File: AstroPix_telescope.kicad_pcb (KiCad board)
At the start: 4 copper layers, 84.3 x 96.1 mm, 14 parts, among them J1 AstroPix2_pcie, J2 AstroPix2_pcie, J3 AstroPix2_pcie, J4 AstroPix2_pcie, P1 pcie_GECCO

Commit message: Resolved spaghetti madness and matched line length as much as possible.
Fabrication outputs prepared, yet again.
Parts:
- moved R2 0.20 mm to (135.0, 99.3)
- moved R4 0.20 mm to (136.0, 79.3)
- moved R6 0.20 mm to (136.0, 59.8)
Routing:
- net /sample_clk0_N: track 163.8 -> 95.7 mm
- net /sample_clk0_P: track 163.7 -> 95.7 mm
- net /sample_clk2_P: track 164.4 -> 120.7 mm
- net /sample_clk2_N: track 164.3 -> 120.6 mm
- net /sample_clk3_P: track 164.8 -> 145.7 mm
- net /sample_clk3_N: track 164.6 -> 145.5 mm
- net /spi3_miso1: track 37.6 -> 41.3 mm
- net /spi3_mosi: track 39.4 -> 42.1 mm
- net /spi_right_mosi: track 117.6 -> 119.9 mm
- net /sr_sin: track 35.5 -> 37.8 mm
- net /spi_right_clk: track 117.6 -> 119.6 mm
- net /spi_right_miso0: track 117.6 -> 119.6 mm
- net /spi2_csn: track 46.3 -> 44.4 mm
- net /spi2_miso1: track 42.0 -> 40.5 mm
- net /sr_ck2: track 223.6 -> 222.3 mm
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
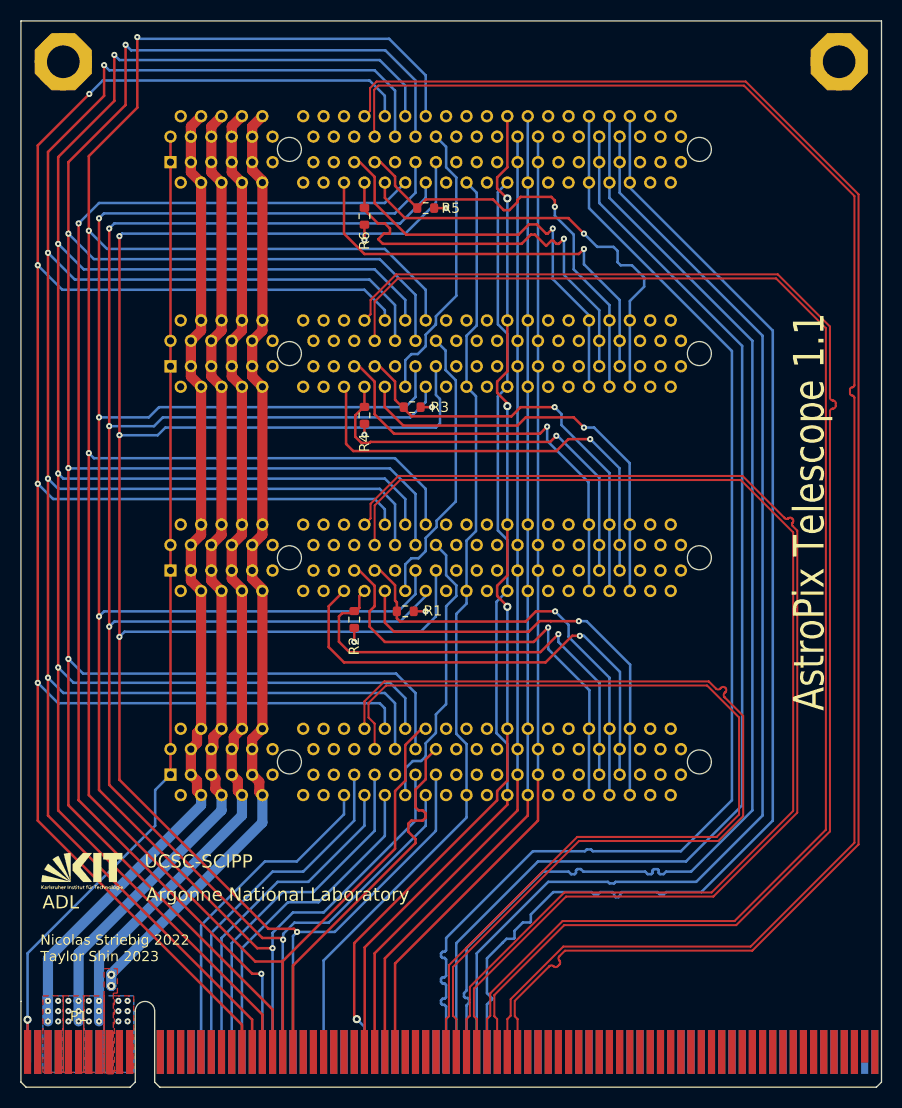
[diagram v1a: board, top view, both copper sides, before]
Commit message: Updated with normalized differential pair length for each PCI-e ports.
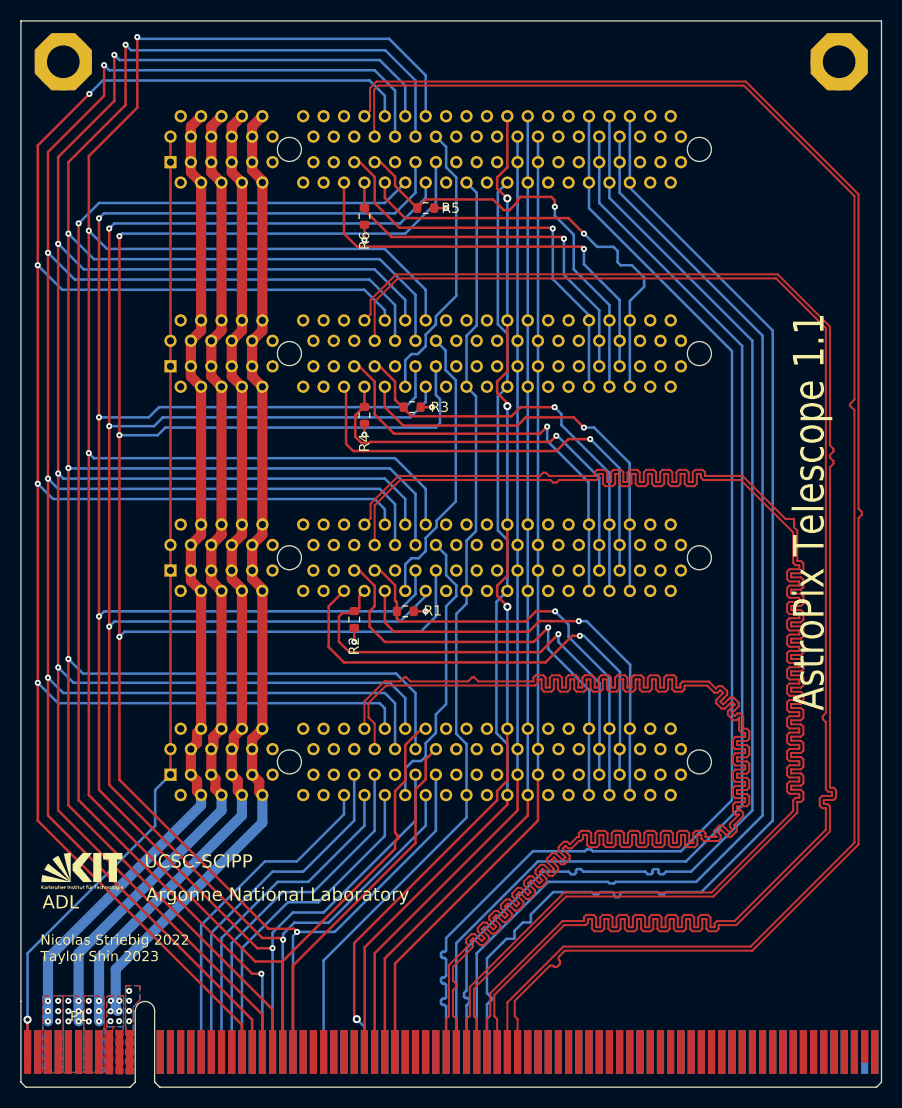
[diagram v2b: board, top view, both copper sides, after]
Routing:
- net /sample_clk0_P: track 95.7 -> 165.1 mm
- net /sample_clk0_N: track 95.7 -> 165.0 mm
- net /sample_clk2_P: track 120.7 -> 165.3 mm
- net /sample_clk2_N: track 120.6 -> 165.2 mm
- net /sample_clk3_N: track 145.5 -> 164.6 mm
- net /sample_clk3_P: track 145.7 -> 164.5 mm
- net /spi3_miso1: track 41.3 -> 37.1 mm
- net VSSA: track 94.6 -> 97.0 mm, vias 2 -> 6
- net /sr_sin: track 37.8 -> 35.5 mm
- net /spi3_clk: track 41.5 -> 40.3 mm
- net GND: vias 12 -> 10
- added copper zone on B.Cu, net VSSA
